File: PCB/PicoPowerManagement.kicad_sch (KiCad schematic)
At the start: 5 parts, among them J1 Raspberry Pi 5 GPIO, J2 Raspberry Pi Pico, J3 NAS Fan 1, J4 NAS Fan 2, J6 Molex Power

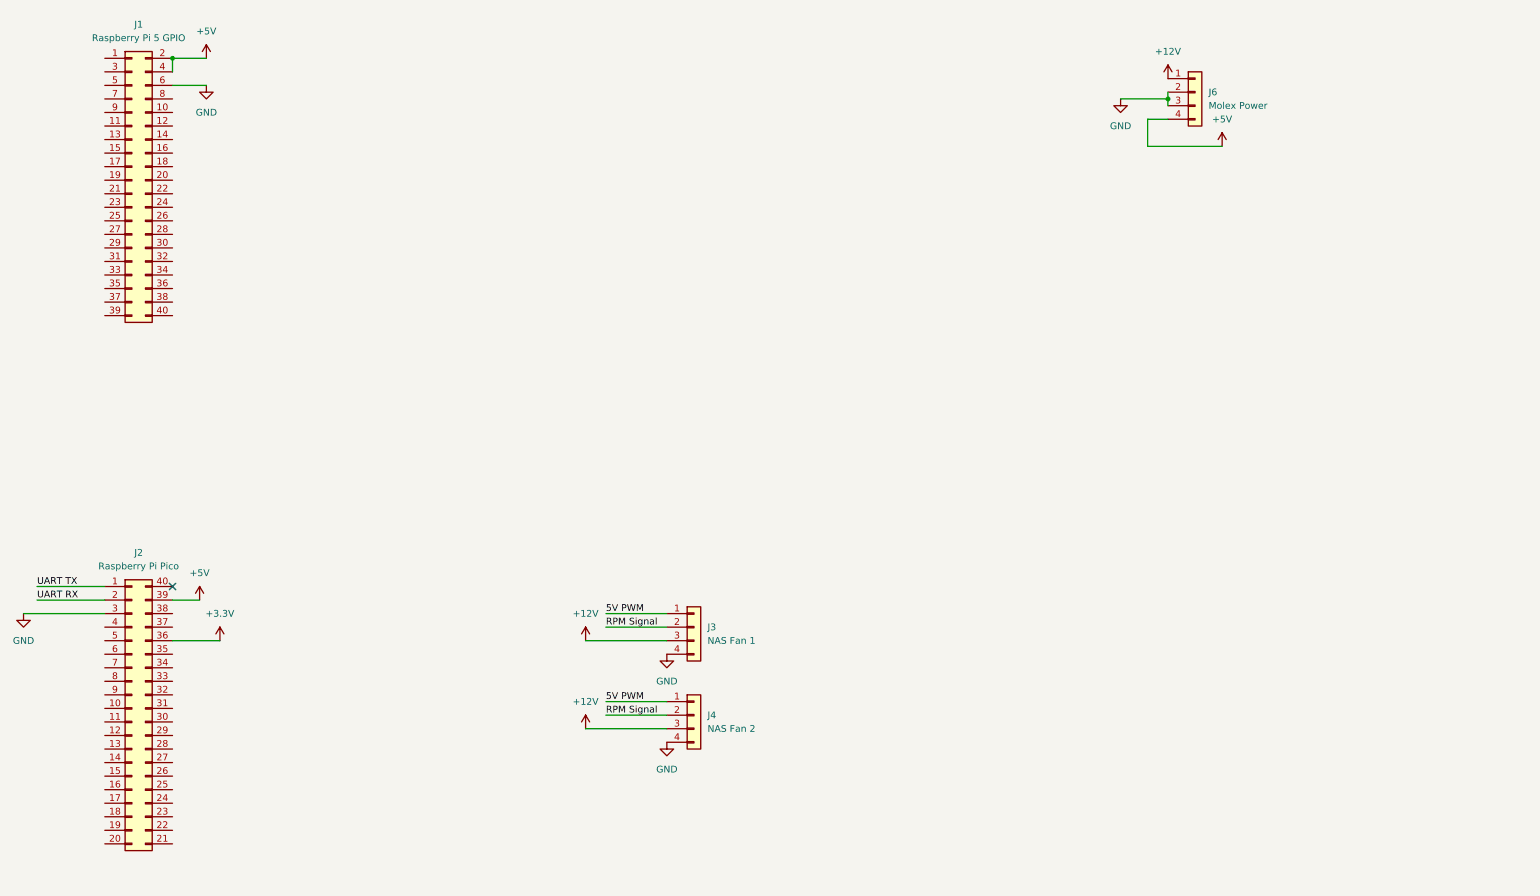
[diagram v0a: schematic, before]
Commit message: Add footprint and symbol libraries for LSF0101DRYR and LSF0102DCUR components
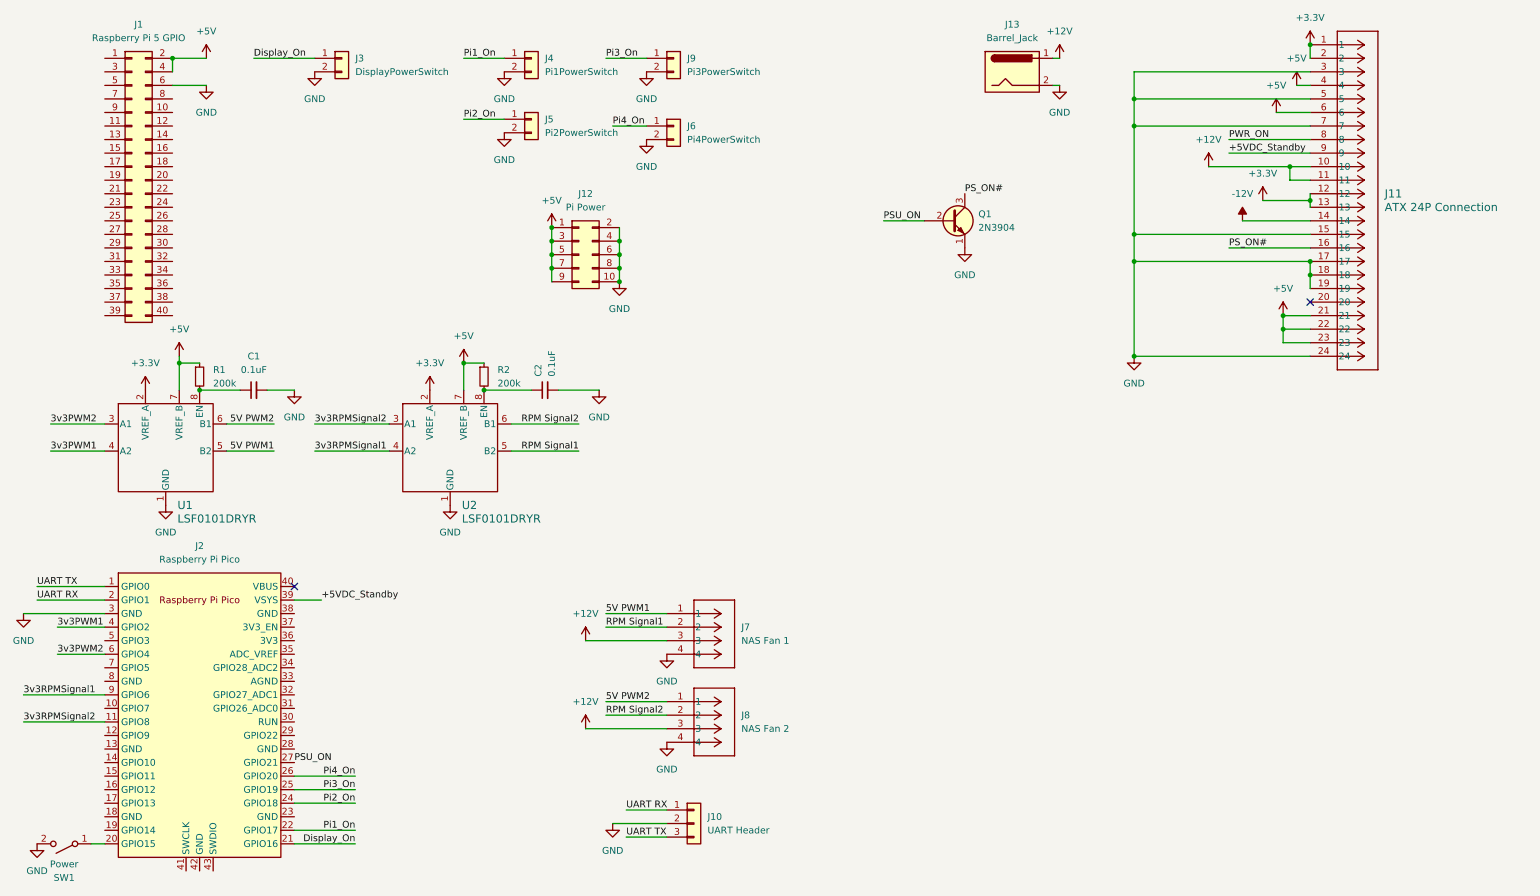
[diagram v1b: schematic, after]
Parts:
- removed J6: Molex Power, symbol Connector_Generic:Conn_01x04
- added C1, C2: 0.1uF, Capacitor_SMD:C_0603_1608Metric_Pad1.08x0.95mm_HandSolder, symbol Device:C_Small
- added J10: UART Header, Connector_PinHeader_2.54mm:PinHeader_1x03_P2.54mm_Vertical, symbol Connector_Generic:Conn_01x03
- added J11: ATX 24P Connection, Mini-fit Jr:CONN_5566-24_MOL, symbol Mini-Fit Jr.:39281243
- added J12: Pi Power, Connector_PinHeader_2.54mm:PinHeader_2x05_P2.54mm_Vertical, symbol Connector_Generic:Conn_02x05_Odd_Even
- added J13: Barrel_Jack, Connector_BarrelJack:BarrelJack_Wuerth_694108106102_2.5x5.5mm, symbol Connector:Barrel_Jack
- added J3: DisplayPowerSwitch, Connector_PinHeader_2.54mm:PinHeader_1x02_P2.54mm_Vertical, symbol Connector_Generic:Conn_01x02
- added J4: Pi1PowerSwitch, Connector_PinHeader_2.54mm:PinHeader_1x02_P2.54mm_Vertical, symbol Connector_Generic:Conn_01x02
- added J5: Pi2PowerSwitch, Connector_PinHeader_2.54mm:PinHeader_1x02_P2.54mm_Vertical, symbol Connector_Generic:Conn_01x02
- added J6: Pi4PowerSwitch, Connector_PinHeader_2.54mm:PinHeader_1x02_P2.54mm_Vertical, symbol Connector_Generic:Conn_01x02
- added J9: Pi3PowerSwitch, Connector_PinHeader_2.54mm:PinHeader_1x02_P2.54mm_Vertical, symbol Connector_Generic:Conn_01x02
- added Q1: 2N3904, PCM_Package_TO_SOT_THT_AKL:TO-92_Inline_Wide_EBC, symbol PCM_Transistor_BJT_AKL:2N3904
- added R1, R2: 200k, Resistor_SMD:R_0603_1608Metric_Pad0.98x0.95mm_HandSolder, symbol Device:R_Small
- added SW1: Power, Connector_PinHeader_2.54mm:PinHeader_1x02_P2.54mm_Vertical, symbol Switch:SW_SPST
- added U1, U2: LSF0101DRYR, LSF0102DCUR:DCU0008A_L, symbol LSF0102DCUR:LSF0102DCUR
- J1: footprint (none) -> Connector_PinHeader_2.54mm:PinHeader_2x20_P2.54mm_Vertical
- J2: footprint (none) -> MCU_RaspberryPi_and_Boards:RPi_Pico_SMD_TH; symbol Connector_Generic:Conn_02x20_Counter_Clockwise -> MCU_RaspberryPi_and_Boards:Pico
- J7: renamed from J3; footprint (none) -> Fan Connector:CONN_SD-47053-001_H10p00_MOL; symbol Connector_Generic:Conn_01x04 -> Fan Connector:470531000
- J8: renamed from J4; footprint (none) -> Fan Connector:CONN_SD-47053-001_H10p00_MOL; symbol Connector_Generic:Conn_01x04 -> Fan Connector:470531000
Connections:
- net +12V: now also J11.10, J11.11, J13.1
- net +3.3V: now also J11.1, J11.12, J11.13, J11.2, U1.2 (VREF_A), U2.2 (VREF_A); no longer J2.36 (Pin_36)
- net +5V: now also J11.21, J11.22, J11.23, J11.4, J11.6, J12.1 (Pin_1), J12.3 (Pin_3), J12.5 (Pin_5), J12.7 (Pin_7), J12.9 (Pin_9), R1.1, R2.1, U1.7 (VREF_B), U2.7 (VREF_B); no longer J2.39 (Pin_39)
- net GND: now also C1.2, C2.2, J10.2 (Pin_2), J11.15, J11.17, J11.18, J11.19, J11.24, J11.3, J11.5, J11.7, J12.10 (Pin_10), J12.2 (Pin_2), J12.4 (Pin_4), J12.6 (Pin_6), J12.8 (Pin_8), J13.2, J3.2 (Pin_2), J4.2 (Pin_2), J5.2 (Pin_2), J6.2 (Pin_2), J9.2 (Pin_2), Q1.1 (E), SW1.2 (B), U1.1 (GND), U2.1 (GND)
- net UART RX: now also J10.1 (Pin_1)
- net UART TX: now also J10.3 (Pin_3)
- net 3v3RPMSignal2: now reaches J2.11 (GPIO8)
- net 3v3RPMSignal2: now also U2.3 (A1)
- net at J2.20 (GPIO15): now also SW1.1 (A)
- net Display_On: now reaches J2.21 (GPIO16)
- net Display_On: now also J3.1 (Pin_1)
- net Pi1_On: now reaches J2.22 (GPIO17)
- net Pi1_On: now also J4.1 (Pin_1)
- net Pi2_On: now reaches J2.24 (GPIO18)
- net Pi2_On: now also J5.1 (Pin_1)
- net Pi3_On: now reaches J2.25 (GPIO19)
- net Pi3_On: now also J9.1 (Pin_1)
- net Pi4_On: now reaches J2.26 (GPIO20)
- net Pi4_On: now also J6.1 (Pin_1)
- net PSU_ON: now reaches J2.27 (GPIO21)
- net PSU_ON: now also Q1.2 (B)
- net 3v3PWM1: now reaches J2.4 (GPIO2)
- net 3v3PWM1: now also U1.4 (A2)
- net 3v3PWM2: now reaches J2.6 (GPIO4)
- net 3v3PWM2: now also U1.3 (A1)
- net 3v3RPMSignal1: now reaches J2.9 (GPIO6)
- net 3v3RPMSignal1: now also U2.4 (A2)
- net 5V PWM renamed 5V PWM1
- net 5V PWM1: now also U1.5 (B2); no longer J8.1 (Pin_1)
- net RPM Signal renamed RPM Signal1
- net RPM Signal1: now also U2.5 (B2); no longer J8.2 (Pin_2)
- new net: C2.1, R2.2, U2.8 (EN)
- new net: C1.1, R1.2, U1.8 (EN)
- new net +5VDC_Standby: J11.9, J2.39 (VSYS)
- new net -12V: J11.14
- new net 5V PWM2: J8.1, U1.6 (B1)
- new net PS_ON#: J11.16, Q1.3 (C)
- new net PWR_ON: J11.8
- new net RPM Signal2: J8.2, U2.6 (B1)
- no-connect marks 1 -> 2

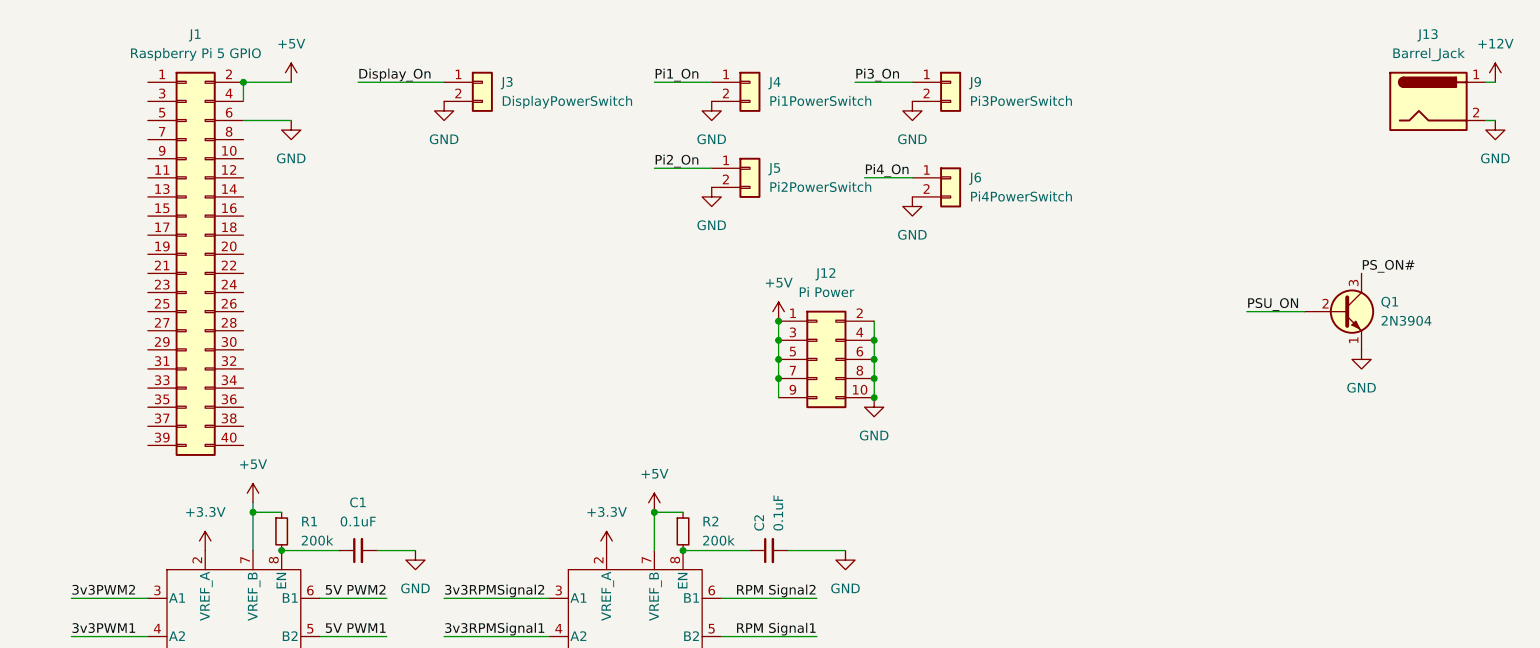
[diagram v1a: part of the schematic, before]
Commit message: Add initial implementation of PicoPowerManagement project with API and client setup
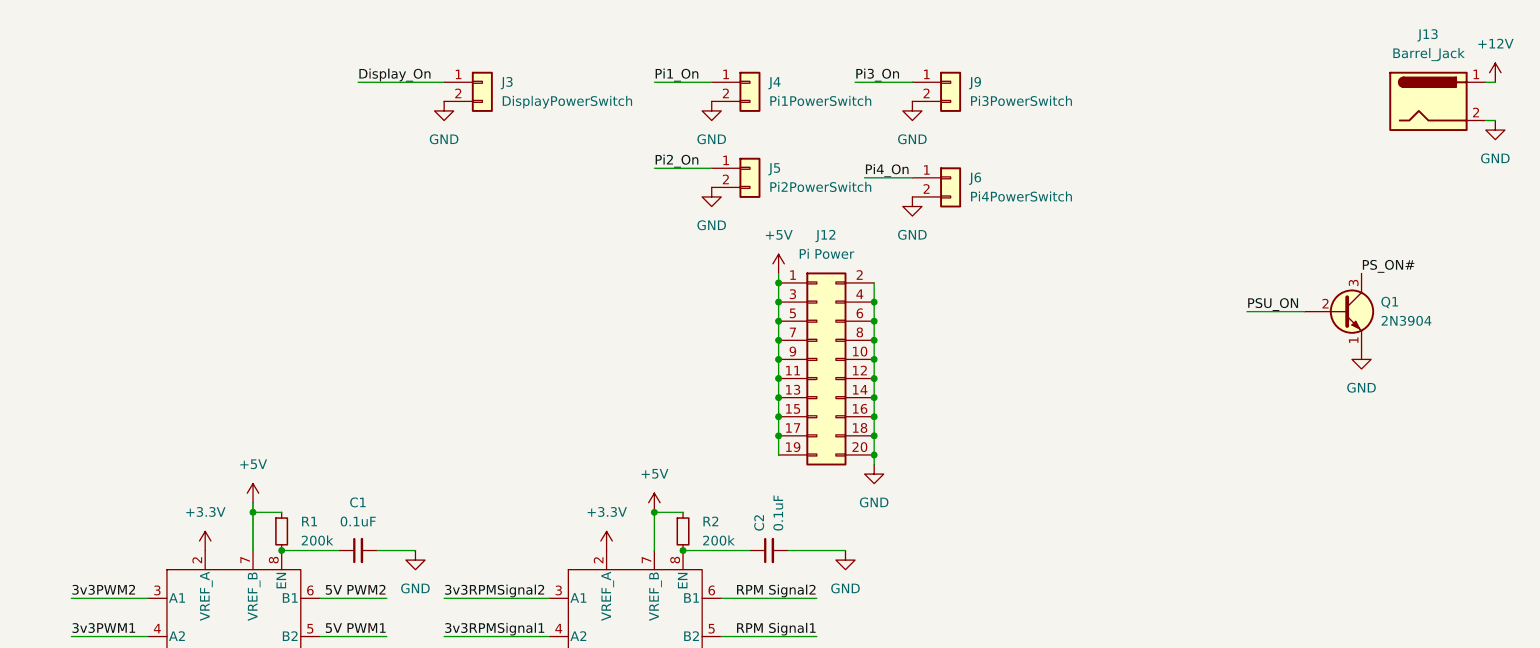
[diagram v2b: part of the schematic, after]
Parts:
- removed J1: Raspberry Pi 5 GPIO, Connector_PinHeader_2.54mm:PinHeader_2x20_P2.54mm_Vertical, symbol Connector_Generic:Conn_02x20_Odd_Even
- J12: footprint Connector_PinHeader_2.54mm:PinHeader_2x05_P2.54mm_Vertical -> Connector_PinHeader_2.54mm:PinHeader_2x10_P2.54mm_Vertical; symbol Connector_Generic:Conn_02x05_Odd_Even -> Connector_Generic:Conn_02x10_Odd_Even
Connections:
- net +5V: now also J12.11 (Pin_11), J12.13 (Pin_13), J12.15 (Pin_15), J12.17 (Pin_17), J12.19 (Pin_19)
- net GND: now also J12.12 (Pin_12), J12.14 (Pin_14), J12.16 (Pin_16), J12.18 (Pin_18), J12.20 (Pin_20)

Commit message: Add new pages and components for PicoPowerManagement client, update libraries, and modify project settings
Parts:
- removed J12: Pi Power, Connector_PinHeader_2.54mm:PinHeader_2x10_P2.54mm_Vertical, symbol Connector_Generic:Conn_02x10_Odd_Even
- removed J13: Barrel_Jack, Connector_BarrelJack:BarrelJack_Wuerth_694108106102_2.5x5.5mm, symbol Connector:Barrel_Jack
- removed J2: Raspberry Pi Pico, MCU_RaspberryPi_and_Boards:RPi_Pico_SMD_TH, symbol MCU_RaspberryPi_and_Boards:Pico
- added C35, C36: 0.1uF, symbol Device:C_Small
- added D1, D2, D3, D4: D_Small, symbol Device:D_Small
- added J2: DEBUG, symbol Connector_Generic:Conn_01x03
- added Q14, Q15: NMOS, symbol Simulation_SPICE:NMOS
- added Q2, Q3: PMOS, symbol Simulation_SPICE:PMOS
- added R10, R11, R3: 4.7k, symbol Device:R_Small
- added R12, R13: 0.25, symbol Device:R_Small
- added U13, U14: LM338T, T03B_TEX, symbol LM338:LM338T_NOPB
- added U6, U7, U8: FUSB302MPX, FUSB302:MLP14_2P5X2P5_ONS, symbol FUSB302:FUSB302MPX
- added U9: ~, symbol MCU_RaspberryPi_and_Boards:PGA2350
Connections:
- net +12V: now also C35.1, U13.3 (IN)
- net +3.3V: now also R10.1, R11.1, U9.56 (3v3)
- net +5V: now also C36.1, U14.3 (IN)
- net +5VDC_Standby: now also U9.57 (VBUS)
- net 3v3PWM1: now also U2.3 (A1), U9.2 (GPIO2); no longer U1.4 (A2)
- net 3v3PWM2: now also U9.4 (GPIO4)
- net 3v3RPMSignal1: now also U9.3 (GPIO3)
- net 3v3RPMSignal2: now also U1.4 (A2), U9.5 (GPIO5); no longer U2.3 (A1)
- net 5V PWM1: now also U2.6 (B1); no longer U1.5 (B2)
- net Display_On: now also U9.6 (GPIO6)
- net GND: now also C35.2, C36.2, J2.2 (Pin_2), Q14.3 (S), Q15.3 (S), R3.2, U9.58 (GND), U9.59 (GND), U9.60 (GND), U9.61 (GND), U9.62 (GND), U9.63 (GND)
- net PSU_ON: now also U9.11 (GPIO11)
- net Pi1_On: now also U9.7 (GPIO7)
- net Pi2_On: now also U9.8 (GPIO8)
- net Pi3_On: now also U9.9 (GPIO9)
- net Pi4_On: now also U9.10 (GPIO10)
- net RPM Signal2: now also U1.5 (B2); no longer U2.6 (B1)
- net UART RX: now also U9.1 (GPIO1)
- net UART TX: now also U9.0 (GPIO0)
- net PWR: now reaches SW1.1 (A)
- net PWR: now also U9.24 (GPIO24)
- new net: D1.2 (A), Q3.1 (D)
- new net: R13.2, U14.1 (ADJ)
- new net: Q2.3 (S), R13.1, U14.2 (OUT)
- new net: D2.2 (A), Q2.1 (D)
- new net: D4.1 (K), Q14.2 (G)
- new net: Q14.1 (D), Q2.2 (G), R11.2
- new net: Q3.3 (S), R12.1, U13.2 (OUT)
- new net: R12.2, U13.1 (ADJ)
- new net: U7.15 (EPAD), U8.2 (VBUS)
- new net: U7.14 (CC2), U8.3 (VDD)
- new net: U7.13 (VCONN), U8.4 (VDD)
- new net: U7.12 (VCONN), U8.5 (INT_N)
- new net: U7.11 (CC1), U8.6 (SCL)
- new net: U7.10 (CC1), U8.7 (SDA)
- new net: D3.1 (K), Q15.2 (G)
- new net: Q15.1 (D), Q3.2 (G), R10.2
- new net BOOTSEL: U9.48 (BOOTSEL)
- new net RESET: U9.53 (RUN)
- new net SCL0: U9.21 (GPIO21)
- new net SCL1: U9.23 (GPIO23)
- new net SDA0: U9.20 (GPIO20)
- new net SDA1: U9.22 (GPIO22)
- new net SWCLK: J2.3 (Pin_3), U9.52 (SWCLK)
- new net SWDIO: J2.1 (Pin_1), U9.49 (SWDIO)
- new net USB0_INT: U9.25 (GPIO25)
- new net USB0_V: D3.2 (A), D4.2 (A), R3.1, U9.31 (GPIO31)
- new net USB0_VBUS: D1.1 (K), D2.1 (K)
- new net USB1_INT: U9.26 (GPIO26)
- new net USB1_V: U9.32 (GPIO32)
- new net USB2_INT: U9.27 (GPIO27)
- new net USB2_V: U9.33 (GPIO33)
- new net USB3_INT: U9.28 (GPIO28)
- new net USB3_V: U9.34 (GPIO34)
- new net USB4_INT: U9.29 (GPIO29)
- new net USB4_V: U9.35 (GPIO35)
- new net USB5_INT: U9.30 (GPIO30)
- new net USB5_V: U9.36 (GPIO36)
- new net USBD+: U9.51 (USBDP)
- new net USBD-: U9.50 (USBDM)
- no-connect marks 2 -> 11
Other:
- added sheet USB0 (USB0.kicad_sch)
- added sheet USB1 (USB1.kicad_sch)
- moved on the sheet: C1, C2, J11, J3, J4, J5, J6, J7, J8, J9, Q1, R1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

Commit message: No code changes made.
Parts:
- removed D3, D4: D_Small, symbol Device:D_Small
- removed Q14, Q15: NMOS, symbol Simulation_SPICE:NMOS
- removed R11: 4.7k, symbol Device:R_Small
- removed R12, R13: 0.25, symbol Device:R_Small
- R10, R3: value 4.7k -> 0.25
- U13, U14: value LM338T -> LM338T/NOPB
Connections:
- net +12V: now also C36.1, U14.3 (IN); no longer C35.1, U13.3 (IN)
- net +3.3V: no longer R10.1
- net +5V: now also C35.1, U13.3 (IN); no longer C36.1, U14.3 (IN)
- net GND: no longer R3.2
- net USB0_V: no longer R3.1
- net at U14.1 (ADJ): now also R10.1
- net at Q2.3 (S): now also R3.2, U13.2 (OUT); no longer U14.2 (OUT)
- net USB0_5VEN: now reaches Q2.2 (G)
- net at Q3.3 (S): now also R10.2, U14.2 (OUT); no longer U13.2 (OUT)
- net at U13.1 (ADJ): now also R3.1
- net USB0_12VEN: now reaches Q3.2 (G)
- net USB0_12VEN: no longer R10.2

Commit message: revamping
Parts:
- removed C35, C36: 0.1uF, symbol Device:C_Small
- removed D1, D2: D_Small, symbol Device:D_Small
- removed J3: DisplayPowerSwitch, Connector_PinHeader_2.54mm:PinHeader_1x02_P2.54mm_Vertical, symbol Connector_Generic:Conn_01x02
- removed J4: Pi1PowerSwitch, Connector_PinHeader_2.54mm:PinHeader_1x02_P2.54mm_Vertical, symbol Connector_Generic:Conn_01x02
- removed J5: Pi2PowerSwitch, Connector_PinHeader_2.54mm:PinHeader_1x02_P2.54mm_Vertical, symbol Connector_Generic:Conn_01x02
- removed J6: Pi4PowerSwitch, Connector_PinHeader_2.54mm:PinHeader_1x02_P2.54mm_Vertical, symbol Connector_Generic:Conn_01x02
- removed J9: Pi3PowerSwitch, Connector_PinHeader_2.54mm:PinHeader_1x02_P2.54mm_Vertical, symbol Connector_Generic:Conn_01x02
- removed Q2, Q3: PMOS, symbol Simulation_SPICE:PMOS
- removed R10, R3: 0.25, symbol Device:R_Small
- removed SW1: Power, Connector_PinHeader_2.54mm:PinHeader_1x02_P2.54mm_Vertical, symbol Switch:SW_SPST
- removed U13, U14: LM338T/NOPB, T03B_TEX, symbol LM338:LM338T_NOPB
- removed U6, U7, U8: FUSB302MPX, FUSB302:MLP14_2P5X2P5_ONS, symbol FUSB302:FUSB302MPX
- added J3: SwitchLEDS, Connector_PinHeader_2.54mm:PinHeader_2x04_P2.54mm_Vertical, symbol Connector_Generic:Conn_02x04_Odd_Even
- added J4: PowerSwitch, Connector_PinHeader_2.54mm:PinHeader_2x06_P2.54mm_Vertical, symbol Connector_Generic:Conn_02x06_Odd_Even
- added U2, U3: LP5810ADSDR, LP5810:DSD0008B-MFG, symbol LP5810:LP5810ADSDR
- J2: footprint (none) -> Connector_PinHeader_2.54mm:PinHeader_1x03_P2.54mm_Vertical
- Q1: footprint PCM_Package_TO_SOT_THT_AKL:TO-92_Inline_Wide_EBC -> Package_TO_SOT_THT:TO-92-2_Wide
- U1: renamed from U9; footprint (none) -> MCU_RaspberryPi_and_Boards:PGA2350
- renumbered C2 to C1, C1 to C2, J10 to J1, J7 to J5, J8 to J6, J11 to J7, R2 to R1, R1 to R2, U2 to U4, U1 to U5
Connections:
- net USB0_V is gone; now on net USB0_5VEN: U1.31 (GPIO31)
- net +3.3V: now also U2.1 (VCC), U3.1 (VCC)
- net Display_On: now also J4.1 (Pin_1)
- net GND: now also J3.7 (Pin_7), J3.8 (Pin_8), J4.10 (Pin_10), J4.12 (Pin_12), J4.2 (Pin_2), J4.4 (Pin_4), J4.6 (Pin_6), J4.8 (Pin_8), U2.2 (SYNC), U3.2 (SYNC), U3.9 (GND)
- net PWR: now also J4.11 (Pin_11)
- net Pi1_On: now also J4.3 (Pin_3)
- net Pi2_On: now also J4.5 (Pin_5)
- net Pi3_On: now also J4.7 (Pin_7)
- net Pi4_On: now also J4.9 (Pin_9)
- net SCL0: now also U2.3 (SCL)
- net SCL1: now also U3.3 (SCL)
- net SDA0: now also U2.4 (SDA)
- net SDA1: now also U3.4 (SDA)
- net USB0_12VEN: now also U1.37 (GPIO37)
- net USB1_12VEN: now reaches U1.38 (GPIO38)
- net USB2_12VEN: now reaches U1.39 (GPIO39)
- net USB3_12VEN: now reaches U1.40 (GPIO40)
- net USB4_12VEN: now reaches U1.41 (GPIO41)
- net USB5_12VEN: now reaches U1.42 (GPIO42)
- net USB1_V renamed USB1_5VEN
- net USB2_V renamed USB2_5VEN
- net USB3_V renamed USB3_5VEN
- net USB4_V renamed USB4_5VEN
- net USB5_V renamed USB5_5VEN
- new net PWR_B: J3.5 (Pin_5), U2.6 (OUT2)
- new net PWR_G: J3.3 (Pin_3), U2.7 (OUT1)
- new net PWR_R: J3.1 (Pin_1), U2.8 (OUT0)
- new net RESET_B: J3.6 (Pin_6), U3.6 (OUT2)
- new net RESET_G: J3.4 (Pin_4), U3.7 (OUT1)
- new net RESET_R: J3.2 (Pin_2), U3.8 (OUT0)
- no-connect marks 11 -> 18
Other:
- added sheet USB_Power (USBPower.kicad_sch)
- moved on the sheet: J1, J2, J5, J6
